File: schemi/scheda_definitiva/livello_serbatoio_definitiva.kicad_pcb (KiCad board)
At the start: 2 copper layers, 83 x 72 mm, 47 parts, among them J1 USB_B, J2 BTN_LED_GROUP, J3 CONN_LCD, J4 CONN_US, J5 ICSP, J6 Exp_Analog_2, J7 Exp_Analog, SW1 SW_RST, U1 FT232RL, U2 ATmega328P-PU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

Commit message: modifica per seriale - aggiunto elettrolitico per alimentazione - fix test seriale
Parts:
- added C9: 100uF, Capacitor_THT:CP_Radial_D5.0mm_P2.00mm, F.Cu at (151.3, 96.4)
- moved REF** 4.27 mm to (145.5, 110.6)
- moved REF** 4.27 mm to (154.2, 110.3)
- moved C2 3.45 mm to (156.1, 85.5)
- moved C1 3.41 mm to (152.7, 88.0)
- renumbered RTS to TP1, CTS to TP2
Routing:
- net GND: track 45.4 -> 38.8 mm, vias 24 -> 27
- net Net-(C2-Pad1): track 4.88 -> 7.77 mm, vias 1 -> 0
- net VDD: track 244.7 -> 242.1 mm
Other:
- board text added: "Monitor serbatoio v1.0_Rev.B Espandibile"
- board text removed: "Monitor serbatoio v1.0_Rev.A Espandibile"

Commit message: aggiunta ferrite a scheda rev. B
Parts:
- added FB1: MPZ2012, Inductor_SMD:L_0805_2012Metric_Pad1.15x1.40mm_HandSolder, F.Cu at (160.0, 91.9)
- moved F1 0.47 mm to (155.3, 94.2)
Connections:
- J1 pad 1: VBUS -> Net-(FB1-Pad2)
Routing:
- net Net-(FB1-Pad2): track 0.00 -> 2.44 mm
- net VBUS: track 23.4 -> 22.0 mm, vias 0 -> 1
- net VDD: track 242.1 -> 242.6 mm

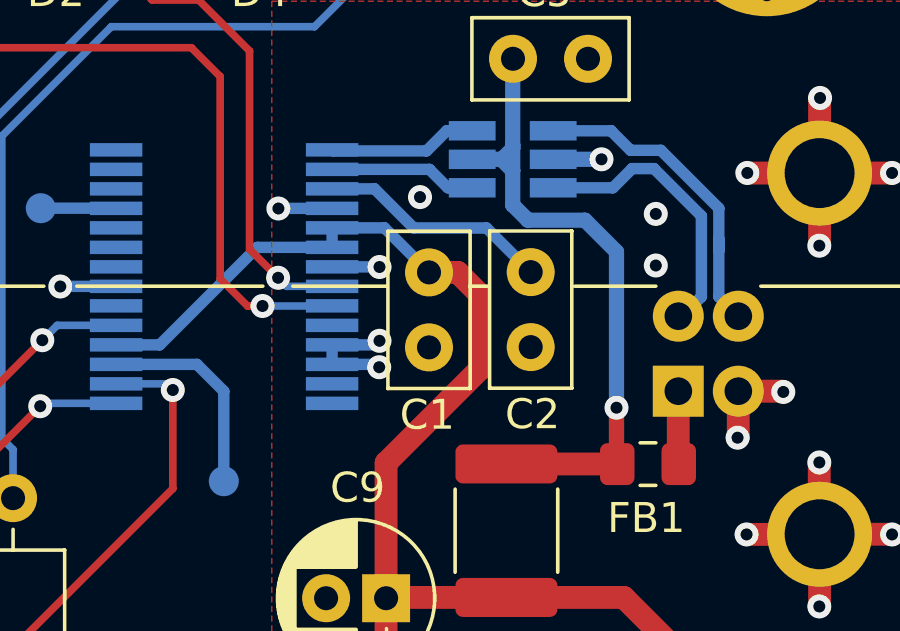
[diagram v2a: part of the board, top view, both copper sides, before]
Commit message: disconnesso pin reset di ft232
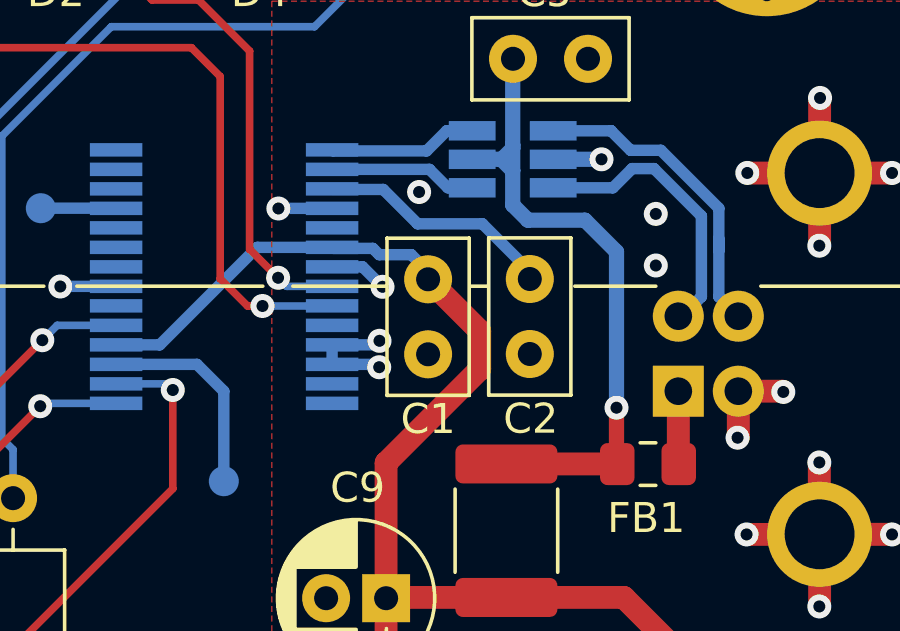
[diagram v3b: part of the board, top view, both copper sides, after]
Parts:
- moved C2 0.23 mm to (156.1, 85.8)
- moved C1 0.23 mm to (152.7, 88.3)
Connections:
- U1 pad 19: VDD -> Net-(U1-Pad19)
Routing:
- net VDD: track 242.6 -> 240.9 mm

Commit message: modifiche scheda definitiva (rev. C)
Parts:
- removed D3: 1N4700, Diode_THT:D_DO-41_SOD81_P7.62mm_Horizontal
- removed J2: BTN_LED_GROUP, simboli_custom:TerminalBlock_RND_205-00047_1x04_P5.00mm_Horizontal
- removed J4: CONN_US, simboli_custom:TerminalBlock_RND_205-00047_1x04_P5.00mm_Horizontal
- removed R11: 10k, Resistor_THT:R_Axial_DIN0309_L9.0mm_D3.2mm_P12.70mm_Horizontal
- added J8: Ext_connections, TerminalBlock_RND:TerminalBlock_RND_205-00051_1x08_P5.00mm_Horizontal, F.Cu at (141.8, 135.4)
- added R5: 10k, Resistor_THT:R_Axial_DIN0309_L9.0mm_D3.2mm_P12.70mm_Horizontal, F.Cu at (137.7, 128.8)
- added REF**: KiCad-Logo2_5mm_SilkScreen, Symbol:KiCad-Logo2_5mm_SilkScreen, F.Cu at (161.2, 89.3)
- C1, C2, C5, C9, F1, FB1: moved to B.Cu
- JP1, JP2, JP3, JP4: moved to F.Cu
- moved R6 51.6 mm to (91.4, 86.1), turned to -90 degrees
- moved R1 37.0 mm to (144.2, 116.8), turned to 90 degrees
- moved R2 35.3 mm to (140.4, 116.8), turned to 90 degrees
- moved C5 34.4 mm to (166.0, 111.8), turned to 90 degrees
- moved J1 33.5 mm to (161.6, 123.0)
- moved J5 31.8 mm to (92.7, 117.1), turned to 180 degrees
- moved REF** 30.8 mm to (157.5, 82.3)
- moved REF** 30.3 mm to (164.9, 81.9)
- moved TP2 30.1 mm to (165.4, 99.4), turned to 180 degrees
- moved U3 29.8 mm to (162.6, 110.7), turned to 90 degrees
- moved J7 26.4 mm to (91.4, 101.9), turned to 180 degrees
- moved R4 23.5 mm to (139.0, 82.6), turned to 0 degrees
- moved C1 23.1 mm to (153.4, 111.4)
- moved C2 22.8 mm to (159.2, 108.3), turned to 180 degrees
- moved R3 21.0 mm to (139.1, 86.5), turned to 0 degrees
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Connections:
- U1 pad 10: Net-(U1-Pad10) -> unconnected-(U1-DCD-Pad10)
- U1 pad 12: Net-(U1-Pad12) -> unconnected-(U1-CBUS4-Pad12)
- U1 pad 13: Net-(U1-Pad13) -> unconnected-(U1-CBUS2-Pad13)
- U1 pad 14: Net-(U1-Pad14) -> unconnected-(U1-CBUS3-Pad14)
- U1 pad 19: Net-(U1-Pad19) -> unconnected-(U1-~{RESET}-Pad19)
- U1 pad 27: Net-(U1-Pad27) -> unconnected-(U1-OSCI-Pad27)
- U1 pad 28: Net-(U1-Pad28) -> unconnected-(U1-OSCO-Pad28)
- U1 pad 6: Net-(U1-Pad6) -> unconnected-(U1-RI-Pad6)
- U1 pad 9: Net-(U1-Pad9) -> unconnected-(U1-DCR-Pad9)
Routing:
- net VDD: track 240.9 -> 287.8 mm
- net GND: track 39.2 -> 5.82 mm, vias 27 -> 34
- net D12: track 53.9 -> 86.6 mm
- net D13: track 34.1 -> 65.6 mm, vias 0 -> 1
- net D11: track 54.3 -> 79.0 mm, vias 0 -> 1
- net Net-(D4-A): track 29.0 -> 5.65 mm
- net Net-(D2-K): track 17.6 -> 39.3 mm
- net Net-(J8-Pin_6): track 18.2 -> 39.6 mm
- net Net-(D1-K): track 24.8 -> 45.2 mm
- net D6: track 50.6 -> 32.8 mm
- net D7: track 49.7 -> 34.0 mm
- net D5: track 48.9 -> 34.0 mm
- net BLA: track 40.6 -> 25.8 mm, vias 1 -> 0
- net D4: track 53.9 -> 39.9 mm
- net D3: track 49.8 -> 37.9 mm
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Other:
- net class Default removed
- board text added: "ECHO"
- board text added: "Monitor serbatoio v1.0_Rev.C Espandibile"
- board text added: "TRIG"
- board text added: "by GR 2023"
- board text removed: "1"
- board text removed: "BTN"
- board text removed: "E"
- board text removed: "Monitor serbatoio v1.0_Rev.B Espandibile"
- board text removed: "SENS"
- board text removed: "T"
- board text removed: "by GR 2021"

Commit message: scheda rev.D - rimosse resistenze RX/TX seriale - aggiustamento label
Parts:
- removed R1, R2: 1k, Resistor_THT:R_Axial_DIN0309_L9.0mm_D3.2mm_P12.70mm_Horizontal
- moved TP1 6.62 mm to (155.8, 95.5)
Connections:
- U1 pad 1: Net-(U1-TXD) -> TX
- U1 pad 5: Net-(U1-RXD) -> RX
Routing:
- net RX: track 37.7 -> 67.1 mm
- net Net-(U1-RXD): track 23.9 -> 0.00 mm
- net TX: track 44.8 -> 68.3 mm
- net Net-(U1-TXD): track 19.0 -> 0.00 mm
- net VDD: track 287.8 -> 303.4 mm
- net DTR: track 69.2 -> 74.0 mm
- net Net-(U1-RTS): track 5.60 -> 2.68 mm
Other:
- board text added: "Monitor serbatoio Rev. D Espandibile"
- board text added: "by GR 2024"
- board text removed: "Monitor serbatoio v1.0_Rev.C Espandibile"
- board text removed: "by GR 2023"

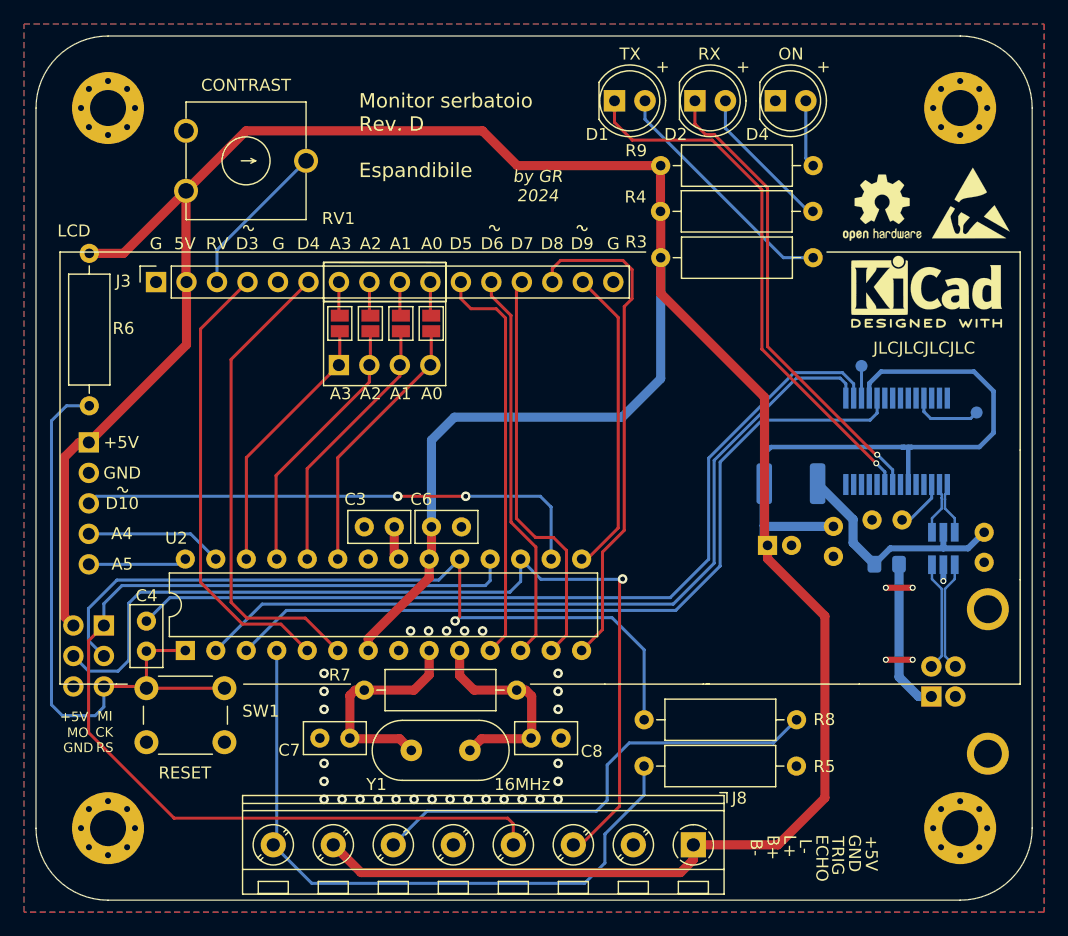
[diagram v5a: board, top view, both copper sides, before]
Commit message: scheda rev. D - applicate revisioni - allineati vincoli a capability jlc - adattata scheda prototipo
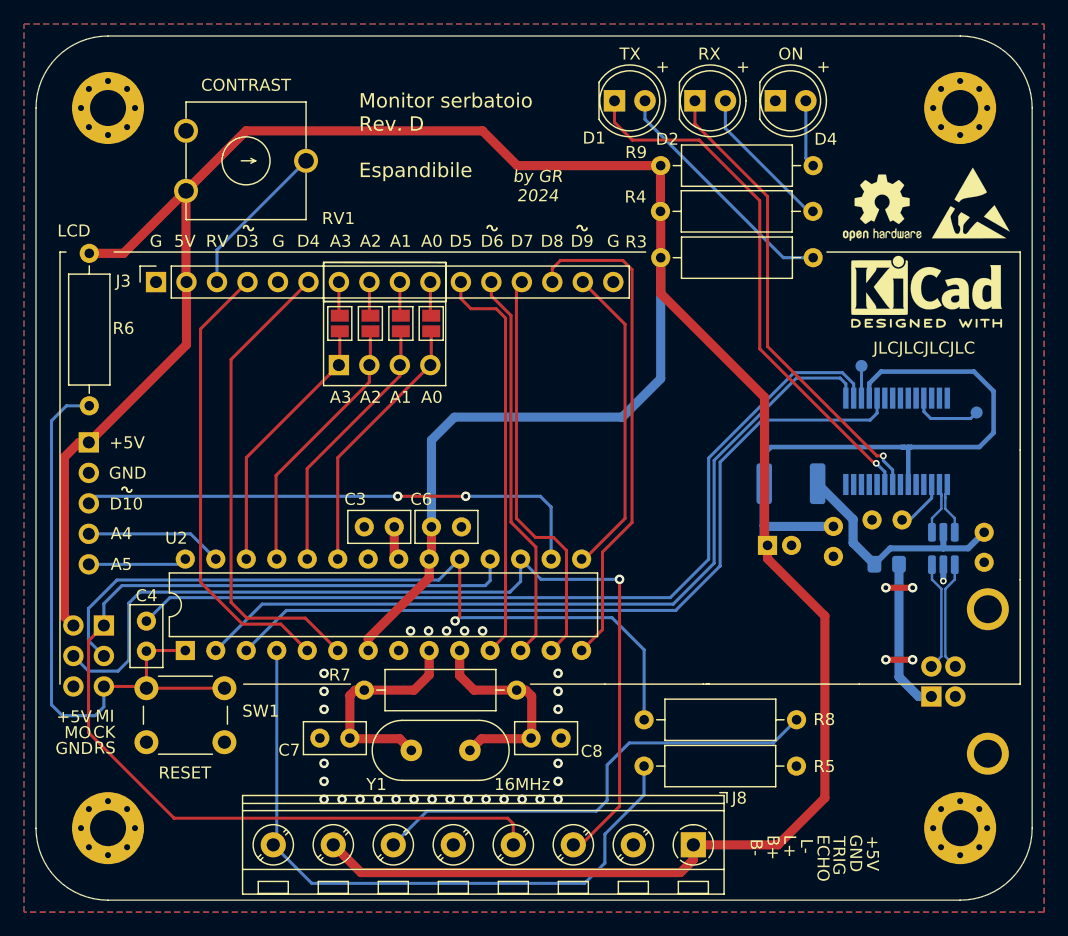
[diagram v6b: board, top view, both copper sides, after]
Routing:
- net Net-(D1-K): track 45.2 -> 44.7 mm

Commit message: corretto schema (placing fuse e condensatori filtro)
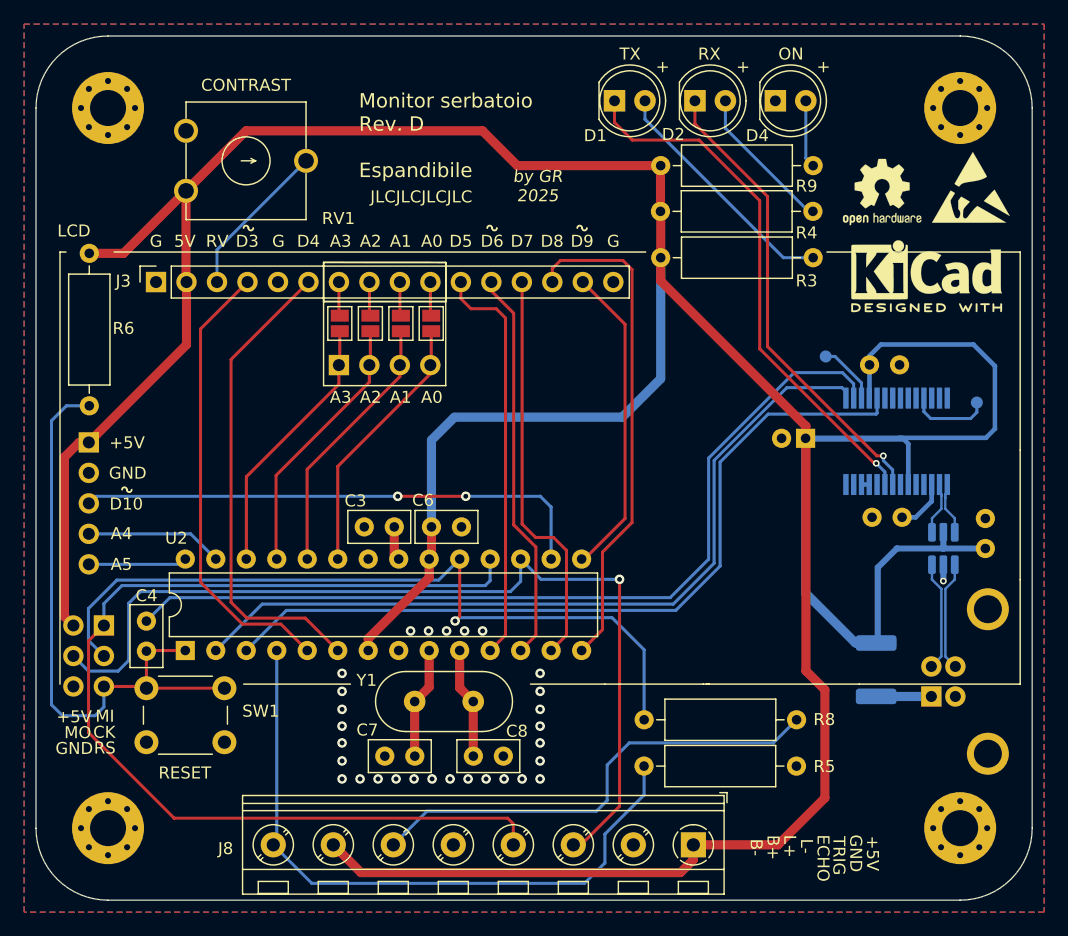
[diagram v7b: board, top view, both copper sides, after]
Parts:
- removed FB1: MPZ2012, Inductor_SMD:L_0805_2012Metric_Pad1.15x1.40mm_HandSolder
- removed R7: 1M, Resistor_THT:R_Axial_DIN0309_L9.0mm_D3.2mm_P12.70mm_Horizontal
- R9: value 1k -> 5k
- moved F1 17.0 mm to (157.0, 120.8), turned to -90 degrees
- moved C1 16.9 mm to (158.9, 95.4), turned to 180 degrees
- moved C9 9.47 mm to (151.1, 101.5), turned to 180 degrees
- moved C7 5.61 mm to (116.1, 128.0)
- moved C8 5.04 mm to (125.9, 128.0)
- moved Y1 4.08 mm to (121.0, 123.5)
- moved C5 3.65 mm to (166.1, 108.2), turned to -90 degrees
- moved TP1 3.08 mm to (152.8, 94.7)
- moved REF** 1.30 mm to (164.9, 80.6)
- moved REF** 1.30 mm to (157.5, 81.0)
- moved REF** 1.30 mm to (161.2, 88.0)
- moved TP2 0.83 mm to (165.4, 98.5)
- moved C2 0.22 mm to (159.2, 108.1)
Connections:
- C5 pad 2: VBUS -> VDD
- F1 pad 2: VBUS -> Net-(J1-VBUS)
- U3 pad 5: VBUS -> VDD
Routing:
- net VDD: track 303.4 -> 328.4 mm
- net VBUS: track 20.3 -> 0.00 mm
- net /X1: track 18.5 -> 8.86 mm
- net /X2: track 17.9 -> 8.80 mm
- net Net-(J1-VBUS): track 12.8 -> 4.60 mm
- net GND: track 5.82 -> 2.56 mm, vias 34 -> 30
- net Net-(U1-RTS): track 2.68 -> 5.16 mm
- net TX: track 68.3 -> 67.3 mm
- net Net-(U1-CTS): track 5.97 -> 6.81 mm
- net Net-(U1-3V3OUT): track 4.35 -> 5.06 mm
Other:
- board text added: "by GR 2025"
- board text removed: "16MHz"
- board text removed: "by GR 2024"

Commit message: revisioni pcb (rimosse violazione jlcpcb) aggiunti stl per case e coperchio da fusion360
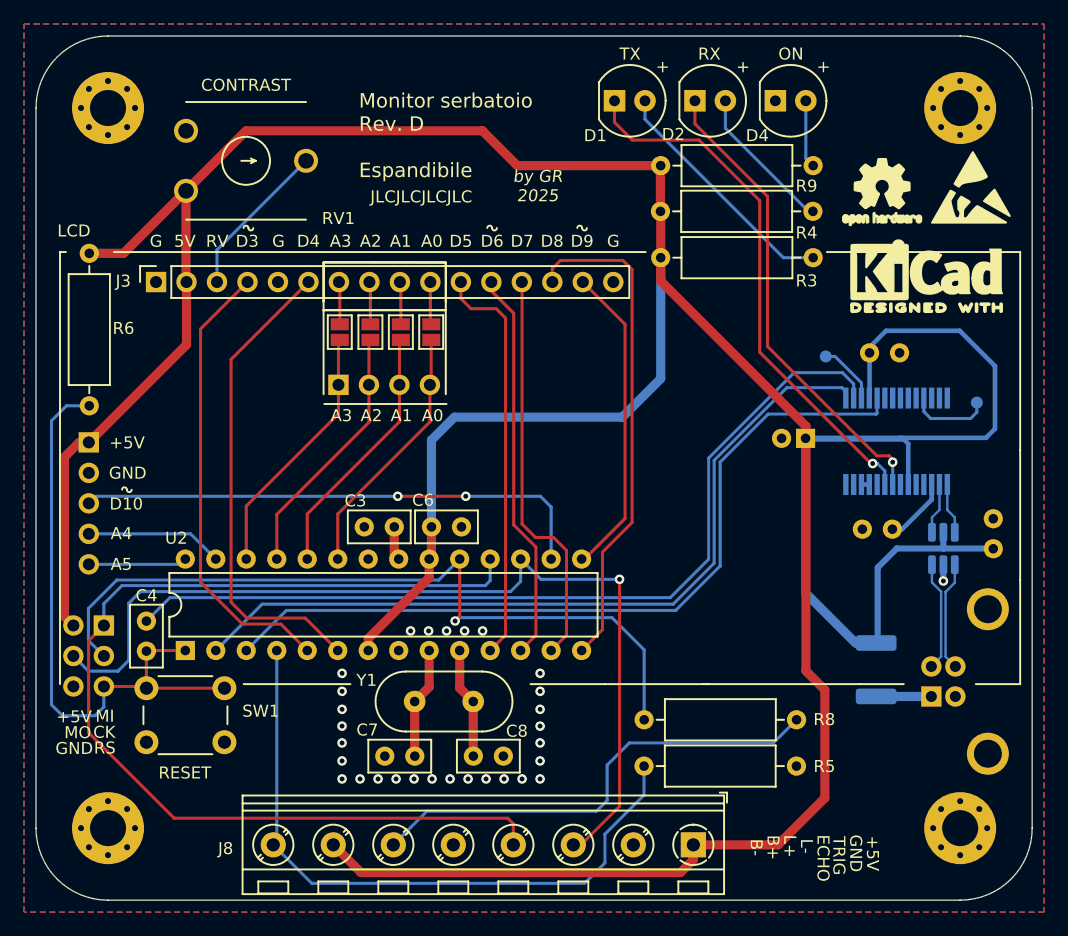
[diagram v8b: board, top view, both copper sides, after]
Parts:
- moved J6 1.65 mm to (112.2, 97.1)
- moved C2 1.28 mm to (158.3, 109.1)
- moved C1 1.00 mm to (158.9, 94.4)
- moved JP1 0.72 mm to (112.3, 92.7)
- moved JP2 0.72 mm to (114.9, 92.7)
- moved JP3 0.72 mm to (117.4, 92.7)
- moved JP4 0.72 mm to (119.9, 92.7)
- moved C5 0.66 mm to (166.8, 108.2)
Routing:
- net VDD: track 328.4 -> 330.3 mm
- net DB2: track 2.83 -> 3.67 mm
- net DB1: track 2.83 -> 3.67 mm
- net DB0: track 2.83 -> 3.65 mm
- net A2: track 22.3 -> 21.5 mm
- net DB3: track 2.83 -> 3.55 mm
- net A0: track 22.2 -> 21.5 mm
- net A3: track 22.2 -> 21.5 mm
- net GND: track 2.56 -> 2.01 mm
- net D_OUT_-: track 5.62 -> 6.14 mm
- net D_OUT_+: track 5.16 -> 5.68 mm
